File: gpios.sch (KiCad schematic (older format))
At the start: 28 parts, among them J1 TB_1X3, J2 TB_1X2, J3 TB_1X2, Q1 BC548, Q2 BC548, U1 4N25, U2 LM35, U3 4N25, U4 RELAY, U5 RELAY

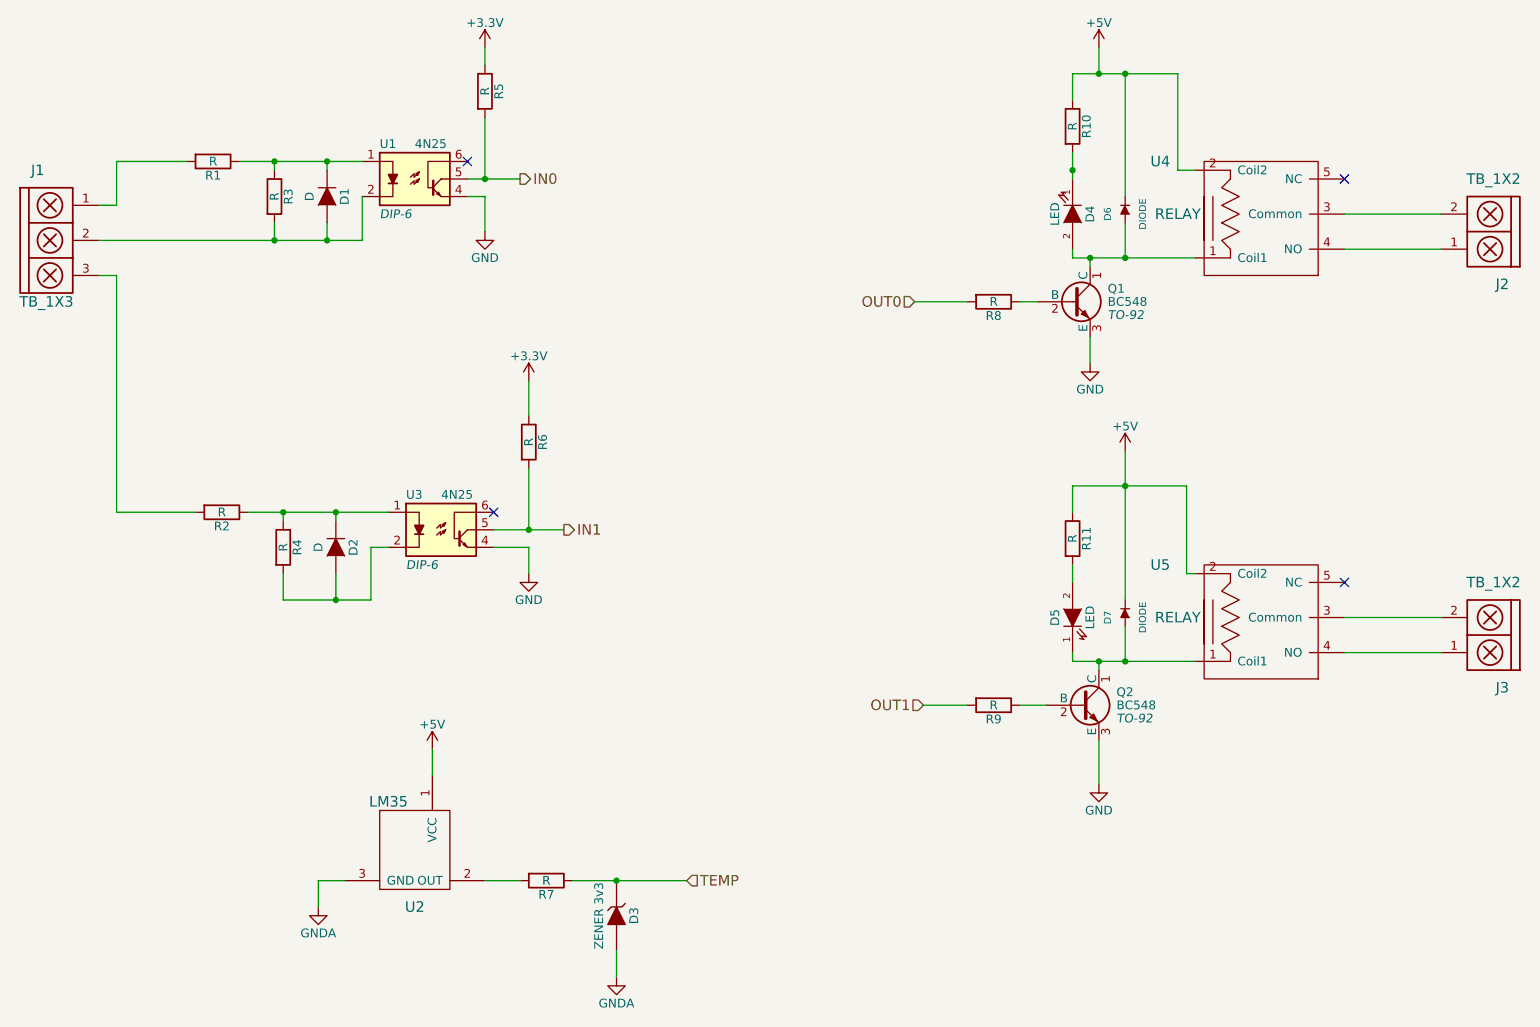
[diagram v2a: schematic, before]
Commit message: se asociaron los footprints menos el modulo
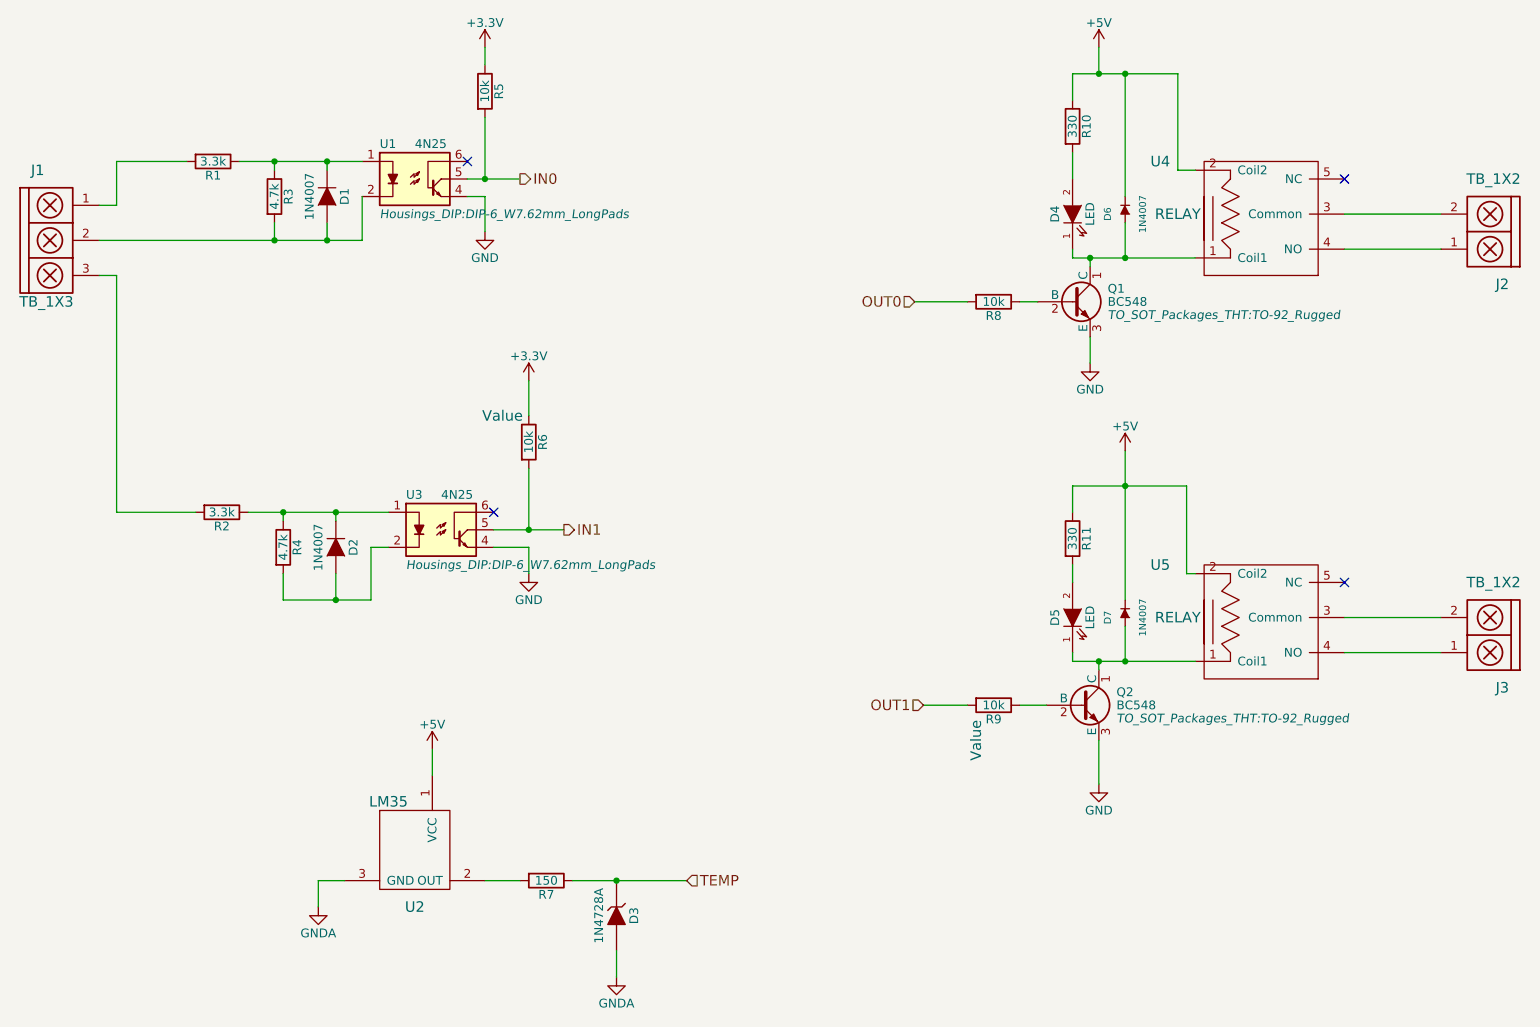
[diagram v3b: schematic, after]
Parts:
- D1, D2: value D -> 1N4007; footprint (none) -> Diodes_THT:Diode_DO-35_SOD27_Horizontal_RM10; Digikey (none) -> Value; Fieldname (none) -> Value
- D3: value ZENER 3v3 -> 1N4728A; footprint (none) -> Diodes_THT:Diode_DO-35_SOD27_Horizontal_RM10; Digikey (none) -> Value; Fieldname (none) -> Value
- D4, D5: footprint (none) -> LEDs:LED-3MM
- D6, D7: value DIODE -> 1N4007; footprint (none) -> Diodes_THT:Diode_DO-35_SOD27_Horizontal_RM10; Digikey (none) -> Value; Fieldname (none) -> Value
- J1: footprint (none) -> ponchoeduciaaiot:bornier3
- J2, J3: footprint (none) -> ponchoeduciaaiot:bornier2
- Q1, Q2: footprint TO-92 -> TO_SOT_Packages_THT:TO-92_Rugged
- R1, R2: value R -> 3.3k; footprint (none) -> Resistors_THT:Resistor_Horizontal_RM7mm; Fieldname (none) -> Value
- R10, R11: value R -> 330; footprint (none) -> Resistors_THT:Resistor_Horizontal_RM7mm; Digikey (none) -> Value; Fieldname (none) -> Value
- R3, R4: value R -> 4.7k; footprint (none) -> Resistors_THT:Resistor_Horizontal_RM7mm; Fieldname (none) -> Value
- R5, R6, R8, R9: value R -> 10k; footprint (none) -> Resistors_THT:Resistor_Horizontal_RM7mm; Digikey (none) -> Value; Fieldname (none) -> Value
- R7: value R -> 150; footprint (none) -> Resistors_THT:Resistor_Horizontal_RM7mm; Digikey (none) -> Value; Fieldname (none) -> Value
- U1, U3: footprint DIP-6 -> Housings_DIP:DIP-6_W7.62mm_LongPads
- U2: footprint (none) -> TO_SOT_Packages_THT:TO-92_Rugged
- U4, U5: footprint (none) -> ponchoeduciaaiot:Relay5vSI
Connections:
- net at D6.1 (A), Q1.1 (C), U4.1 (Coil1): now also D4.1 (K); no longer D4.2 (A)
- net at R10.2: now also D4.2 (A); no longer D4.1 (K)
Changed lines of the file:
@@
 F 0 "J1" H 1300 2300 60  0000 C CNN
 F 1 "TB_1X3" H 1350 1550 60  0000 C CNN
-F 2 "" H 1250 2050 60  0000 C CNN
+F 2 "ponchoeduciaaiot:bornier3" H 1250 2050 60  0001 C CNN
 F 3 "" H 1250 2050 60  0000 C CNN
 	1    1300 2000
@@
 F 0 "J2" H 9650 2350 60  0000 C CNN
 F 1 "TB_1X2" H 9700 1750 60  0000 C CNN
-F 2 "" H 9600 2100 60  0000 C CNN
+F 2 "ponchoeduciaaiot:bornier2" H 9600 2100 60  0001 C CNN
 F 3 "" H 9600 2100 60  0000 C CNN
 	1    9650 2050
@@
 F 0 "J3" H 9650 4650 60  0000 C CNN
 F 1 "TB_1X2" H 9700 4050 60  0000 C CNN
-F 2 "" H 9600 4400 60  0000 C CNN
+F 2 "ponchoeduciaaiot:bornier2" H 9600 4400 60  0001 C CNN
 F 3 "" H 9600 4400 60  0000 C CNN
 	1    9650 4350
@@
 F 0 "U4" H 7700 1650 60  0000 C CNN
 F 1 "RELAY" H 7600 1950 60  0000 C CNN
-F 2 "" H 7700 1650 60  0001 C CNN
+F 2 "ponchoeduciaaiot:Relay5vSI" H 7700 1650 60  0001 C CNN
 F 3 "" H 7700 1650 60  0001 C CNN
 	1    7700 1650
@@
 F 0 "U5" H 7700 3950 60  0000 C CNN
 F 1 "RELAY" H 7600 4250 60  0000 C CNN
-F 2 "" H 7700 3950 60  0001 C CNN
+F 2 "ponchoeduciaaiot:Relay5vSI" H 7700 3950 60  0001 C CNN
 F 3 "" H 7700 3950 60  0001 C CNN
 	1    7700 3950
@@
 F 0 "Q1" H 7400 2525 50  0000 L CNN
 F 1 "BC548" H 7400 2450 50  0000 L CNN
-F 2 "TO-92" H 7400 2375 50  0000 L CIN
+F 2 "TO_SOT_Packages_THT:TO-92_Rugged" H 7400 2375 50  0000 L CIN
 F 3 "" H 7200 2450 50  0000 L CNN
 	1    7200 2450
@@
 F 0 "Q2" H 7450 4825 50  0000 L CNN
 F 1 "BC548" H 7450 4750 50  0000 L CNN
-F 2 "TO-92" H 7450 4675 50  0000 L CIN
+F 2 "TO_SOT_Packages_THT:TO-92_Rugged" H 7450 4675 50  0000 L CIN
 F 3 "" H 7250 4750 50  0000 L CNN
 	1    7250 4750
@@
 P 7500 1950
 F 0 "D6" H 7500 2050 40  0000 C CNN
-F 1 "DIODE" H 7500 1850 40  0000 C CNN
-F 2 "" H 7500 1950 60  0000 C CNN
+F 1 "1N4007" H 7500 1850 40  0000 C CNN
+F 2 "Diodes_THT:Diode_DO-35_SOD27_Horizontal_RM10" H 7500 1950 60  0001 C CNN
 F 3 "" H 7500 1950 60  0000 C CNN
+F 4 "Value" H 7700 2000 60  0001 C CNN "Digikey"
+F 5 "Value" H 7500 1950 60  0001 C CNN "Fieldname"
 	1    7500 1950
 	0    -1   -1   0
@@
 P 7500 4250
 F 0 "D7" H 7500 4350 40  0000 C CNN
-F 1 "DIODE" H 7500 4150 40  0000 C CNN
-F 2 "" H 7500 4250 60  0000 C CNN
+F 1 "1N4007" H 7500 4150 40  0000 C CNN
+F 2 "Diodes_THT:Diode_DO-35_SOD27_Horizontal_RM10" H 7500 4250 60  0001 C CNN
 F 3 "" H 7500 4250 60  0000 C CNN
+F 4 "Value" H 7700 4300 60  0001 C CNN "Digikey"
+F 5 "Value" H 7500 4250 60  0001 C CNN "Fieldname"
 	1    7500 4250
 	0    -1   -1   0
@@
 F 0 "D4" H 7200 2050 50  0000 C CNN
 F 1 "LED" H 7200 1850 50  0000 C CNN
-F 2 "" H 7200 1950 50  0000 C CNN
+F 2 "LEDs:LED-3MM" H 7200 1950 50  0001 C CNN
 F 3 "" H 7200 1950 50  0000 C CNN
 	1    7200 1950
-	0    1    1    0
+	0    -1   -1   0
 $EndComp
 $Comp
@@
 F 0 "D5" H 7200 4350 50  0000 C CNN
 F 1 "LED" H 7200 4150 50  0000 C CNN
-F 2 "" H 7200 4250 50  0000 C CNN
+F 2 "LEDs:LED-3MM" H 7200 4250 50  0001 C CNN
 F 3 "" H 7200 4250 50  0000 C CNN
 	1    7200 4250
@@
 P 7200 1450
 F 0 "R10" V 7280 1450 50  0000 C CNN
-F 1 "R" V 7200 1450 50  0000 C CNN
-F 2 "" V 7130 1450 50  0000 C CNN
+F 1 "330" V 7200 1450 50  0000 C CNN
+F 2 "Resistors_THT:Resistor_Horizontal_RM7mm" V 7130 1450 50  0001 C CNN
 F 3 "" H 7200 1450 50  0000 C CNN
+F 4 "Value" H 7050 1650 60  0001 C CNN "Digikey"
+F 5 "Value" H 7200 1450 60  0001 C CNN "Fieldname"
 	1    7200 1450
 	1    0    0    -1
@@
 P 7200 3800
 F 0 "R11" V 7280 3800 50  0000 C CNN
-F 1 "R" V 7200 3800 50  0000 C CNN
-F 2 "" V 7130 3800 50  0000 C CNN
+F 1 "330" V 7200 3800 50  0000 C CNN
+F 2 "Resistors_THT:Resistor_Horizontal_RM7mm" V 7130 3800 50  0001 C CNN
 F 3 "" H 7200 3800 50  0000 C CNN
+F 4 "Value" H 7050 3950 60  0001 C CNN "Digikey"
+F 5 "Value" H 7200 3800 60  0001 C CNN "Fieldname"
 	1    7200 3800
 	1    0    0    -1
@@
 Wire Wire Line
 	7500 1150 7500 1850
-Connection ~ 7200 1700
 Wire Wire Line
 	7200 1150 7800 1150
@@
 P 6750 2450
 F 0 "R8" V 6830 2450 50  0000 C CNN
-F 1 "R" V 6750 2450 50  0000 C CNN
-F 2 "" V 6680 2450 50  0000 C CNN
+F 1 "10k" V 6750 2450 50  0000 C CNN
+F 2 "Resistors_THT:Resistor_Horizontal_RM7mm" V 6680 2450 50  0001 C CNN
 F 3 "" H 6750 2450 50  0000 C CNN
+F 4 "Value" H 6900 2250 60  0001 C CNN "Digikey"
+F 5 "Value" H 6750 2450 60  0001 C CNN "Fieldname"
 	1    6750 2450
 	0    1    1    0
@@
 P 6750 4750
 F 0 "R9" V 6830 4750 50  0000 C CNN
-F 1 "R" V 6750 4750 50  0000 C CNN
-F 2 "" V 6680 4750 50  0000 C CNN
+F 1 "10k" V 6750 4750 50  0000 C CNN
+F 2 "Resistors_THT:Resistor_Horizontal_RM7mm" V 6680 4750 50  0001 C CNN
 F 3 "" H 6750 4750 50  0000 C CNN
+F 4 "Value" H 6950 4650 60  0000 C CNN "Digikey"
+F 5 "Value" H 6750 4750 60  0001 C CNN "Fieldname"
 	1    6750 4750
 	0    1    1    0
@@
 F 0 "U1" H 3250 1950 50  0000 L CNN
 F 1 "4N25" H 3450 1950 50  0000 L CNN
-F 2 "DIP-6" H 3250 1550 50  0000 L CIN
+F 2 "Housings_DIP:DIP-6_W7.62mm_LongPads" H 3250 1550 50  0000 L CIN
 F 3 "" H 3450 1750 50  0000 L CNN
 	1    3450 1750
@@
 F 0 "U3" H 3400 3950 50  0000 L CNN
 F 1 "4N25" H 3600 3950 50  0000 L CNN
-F 2 "DIP-6" H 3400 3550 50  0000 L CIN
+F 2 "Housings_DIP:DIP-6_W7.62mm_LongPads" H 3400 3550 50  0000 L CIN
 F 3 "" H 3600 3750 50  0000 L CNN
 	1    3600 3750
@@
 P 3850 1250
 F 0 "R5" V 3930 1250 50  0000 C CNN
-F 1 "R" V 3850 1250 50  0000 C CNN
-F 2 "" V 3780 1250 50  0000 C CNN
+F 1 "10k" V 3850 1250 50  0000 C CNN
+F 2 "Resistors_THT:Resistor_Horizontal_RM7mm" V 3780 1250 50  0001 C CNN
 F 3 "" H 3850 1250 50  0000 C CNN
+F 4 "Value" H 3700 1400 60  0001 C CNN "Digikey"
+F 5 "Value" H 3850 1250 60  0001 C CNN "Fieldname"
 	1    3850 1250
 	1    0    0    -1
@@
 P 2300 1650
 F 0 "R1" V 2380 1650 50  0000 C CNN
-F 1 "R" V 2300 1650 50  0000 C CNN
-F 2 "" V 2230 1650 50  0000 C CNN
+F 1 "3.3k" V 2300 1650 50  0000 C CNN
+F 2 "Resistors_THT:Resistor_Horizontal_RM7mm" V 2230 1650 50  0001 C CNN
 F 3 "" H 2300 1650 50  0000 C CNN
+F 4 "Value" H 2300 1650 60  0001 C CNN "Fieldname"
 	1    2300 1650
 	0    1    1    0
@@
 P 2650 1850
 F 0 "R3" V 2730 1850 50  0000 C CNN
-F 1 "R" V 2650 1850 50  0000 C CNN
-F 2 "" V 2580 1850 50  0000 C CNN
+F 1 "4.7k" V 2650 1850 50  0000 C CNN
+F 2 "Resistors_THT:Resistor_Horizontal_RM7mm" V 2580 1850 50  0001 C CNN
 F 3 "" H 2650 1850 50  0000 C CNN
+F 4 "Value" H 2650 1850 60  0001 C CNN "Fieldname"
 	1    2650 1850
 	1    0    0    -1
@@
 P 2950 1850
 F 0 "D1" H 2950 1950 50  0000 C CNN
-F 1 "D" H 2950 1750 50  0000 C CNN
-F 2 "" H 2950 1850 50  0000 C CNN
+F 1 "1N4007" H 2950 1750 50  0000 C CNN
+F 2 "Diodes_THT:Diode_DO-35_SOD27_Horizontal_RM10" H 2950 1850 50  0001 C CNN
 F 3 "" H 2950 1850 50  0000 C CNN
+F 4 "Value" H 2600 1800 60  0001 C CNN "Digikey"
+F 5 "Value" H 2950 1850 60  0001 C CNN "Fieldname"
 	1    2950 1850
 	0    1    1    0
@@
 P 4100 3250
 F 0 "R6" V 4180 3250 50  0000 C CNN
-F 1 "R" V 4100 3250 50  0000 C CNN
-F 2 "" V 4030 3250 50  0000 C CNN
+F 1 "10k" V 4100 3250 50  0000 C CNN
+F 2 "Resistors_THT:Resistor_Horizontal_RM7mm" V 4030 3250 50  0001 C CNN
 F 3 "" H 4100 3250 50  0000 C CNN
+F 4 "Value" H 3950 3400 60  0000 C CNN "Digikey"
+F 5 "Value" H 4100 3250 60  0001 C CNN "Fieldname"
 	1    4100 3250
 	1    0    0    -1
@@
 P 2700 3850
 F 0 "R4" V 2780 3850 50  0000 C CNN
-F 1 "R" V 2700 3850 50  0000 C CNN
-F 2 "" V 2630 3850 50  0000 C CNN
+F 1 "4.7k" V 2700 3850 50  0000 C CNN
+F 2 "Resistors_THT:Resistor_Horizontal_RM7mm" V 2630 3850 50  0001 C CNN
 F 3 "" H 2700 3850 50  0000 C CNN
+F 4 "Value" H 2700 3850 60  0001 C CNN "Fieldname"
 	1    2700 3850
 	1    0    0    -1
@@
 P 2350 3650
 F 0 "R2" V 2430 3650 50  0000 C CNN
-F 1 "R" V 2350 3650 50  0000 C CNN
-F 2 "" V 2280 3650 50  0000 C CNN
+F 1 "3.3k" V 2350 3650 50  0000 C CNN
+F 2 "Resistors_THT:Resistor_Horizontal_RM7mm" V 2280 3650 50  0001 C CNN
 F 3 "" H 2350 3650 50  0000 C CNN
+F 4 "Value" H 2350 3650 60  0001 C CNN "Fieldname"
 	1    2350 3650
 	0    1    1    0
@@
 P 3000 3850
 F 0 "D2" H 3000 3950 50  0000 C CNN
-F 1 "D" H 3000 3750 50  0000 C CNN
-F 2 "" H 3000 3850 50  0000 C CNN
+F 1 "1N4007" H 3000 3750 50  0000 C CNN
+F 2 "Diodes_THT:Diode_DO-35_SOD27_Horizontal_RM10" H 3000 3850 50  0001 C CNN
 F 3 "" H 3000 3850 50  0000 C CNN
+F 4 "Value" H 3450 3800 60  0001 C CNN "Digikey"
+F 5 "Value" H 3000 3850 60  0001 C CNN "Fieldname"
 	1    3000 3850
 	0    1    1    0
@@
 F 0 "U2" H 3450 5900 60  0000 C CNN
 F 1 "LM35" H 3300 6500 60  0000 C CNN
-F 2 "" H 3450 5900 60  0001 C CNN
+F 2 "TO_SOT_Packages_THT:TO-92_Rugged" H 3450 5900 60  0001 C CNN
 F 3 "" H 3450 5900 60  0001 C CNN
 	1    3450 5900
@@
 P 4200 5750
 F 0 "R7" V 4280 5750 50  0000 C CNN
-F 1 "R" V 4200 5750 50  0000 C CNN
-F 2 "" V 4130 5750 50  0000 C CNN
+F 1 "150" V 4200 5750 50  0000 C CNN
+F 2 "Resistors_THT:Resistor_Horizontal_RM7mm" V 4130 5750 50  0001 C CNN
 F 3 "" H 4200 5750 50  0000 C CNN
+F 4 "Value" H 4200 5750 60  0001 C CNN "Fieldname"
+F 5 "Value" H 4000 5650 60  0001 C CNN "Digikey"
 	1    4200 5750
 	0    1    1    0
@@
 P 4600 5950
 F 0 "D3" H 4600 6050 50  0000 C CNN
-F 1 "ZENER 3v3" H 4600 5850 50  0000 C CNN
-F 2 "" H 4600 5950 50  0000 C CNN
+F 1 "1N4728A" H 4600 5850 50  0000 C CNN
+F 2 "Diodes_THT:Diode_DO-35_SOD27_Horizontal_RM10" H 4600 5950 50  0001 C CNN
 F 3 "" H 4600 5950 50  0000 C CNN
+F 4 "Value" H 4800 6100 60  0001 C CNN "Digikey"
+F 5 "Value" H 4600 5950 60  0001 C CNN "Fieldname"
 	1    4600 5950
 	0    1    1    0

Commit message: footprints ok, componentes en pcb
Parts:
- U2: Fieldname (none) -> Value
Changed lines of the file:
@@
 F 2 "TO_SOT_Packages_THT:TO-92_Rugged" H 3450 5900 60  0001 C CNN
 F 3 "" H 3450 5900 60  0001 C CNN
+F 4 "Value" H 3450 5900 60  0001 C CNN "Fieldname"
 	1    3450 5900
 	1    0    0    -1
